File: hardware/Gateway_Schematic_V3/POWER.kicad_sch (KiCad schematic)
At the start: 49 parts, among them J3 Screw_Terminal_01x03, U11 TPS5430DDA, U4 AMS1117-3.3, U7 TPS5430DDA

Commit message: Update PCB Layout for Gateway (24/3/2026)
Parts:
- TP1, TP13: footprint TestPoint:TestPoint_Pad_D1.0mm -> IVS_NEW_FOOTPRINT:TestPoint_throughtHole_D1.0mm
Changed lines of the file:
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@@
 			)
 		)
-		(property "Footprint" "TestPoint:TestPoint_Pad_D1.0mm"
+		(property "Footprint" "IVS_NEW_FOOTPRINT:TestPoint_throughtHole_D1.0mm"
 			(at 144.145 104.14 0)
 			(effects
@@
 			)
 		)
-		(property "Footprint" "TestPoint:TestPoint_Pad_D1.0mm"
+		(property "Footprint" "IVS_NEW_FOOTPRINT:TestPoint_throughtHole_D1.0mm"
 			(at 294.005 40.64 0)
 			(effects

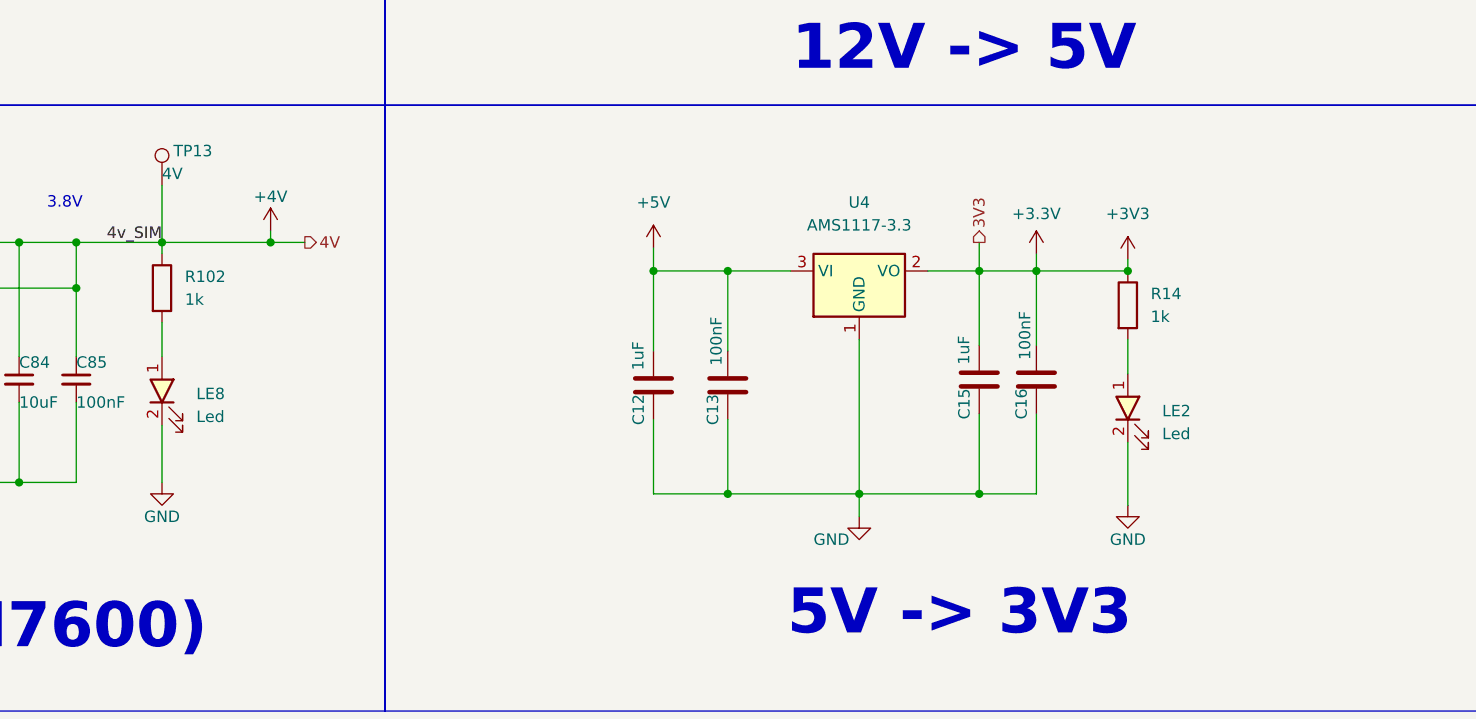
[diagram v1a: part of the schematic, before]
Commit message: Update Solder Bridge for 3v3 and 4v
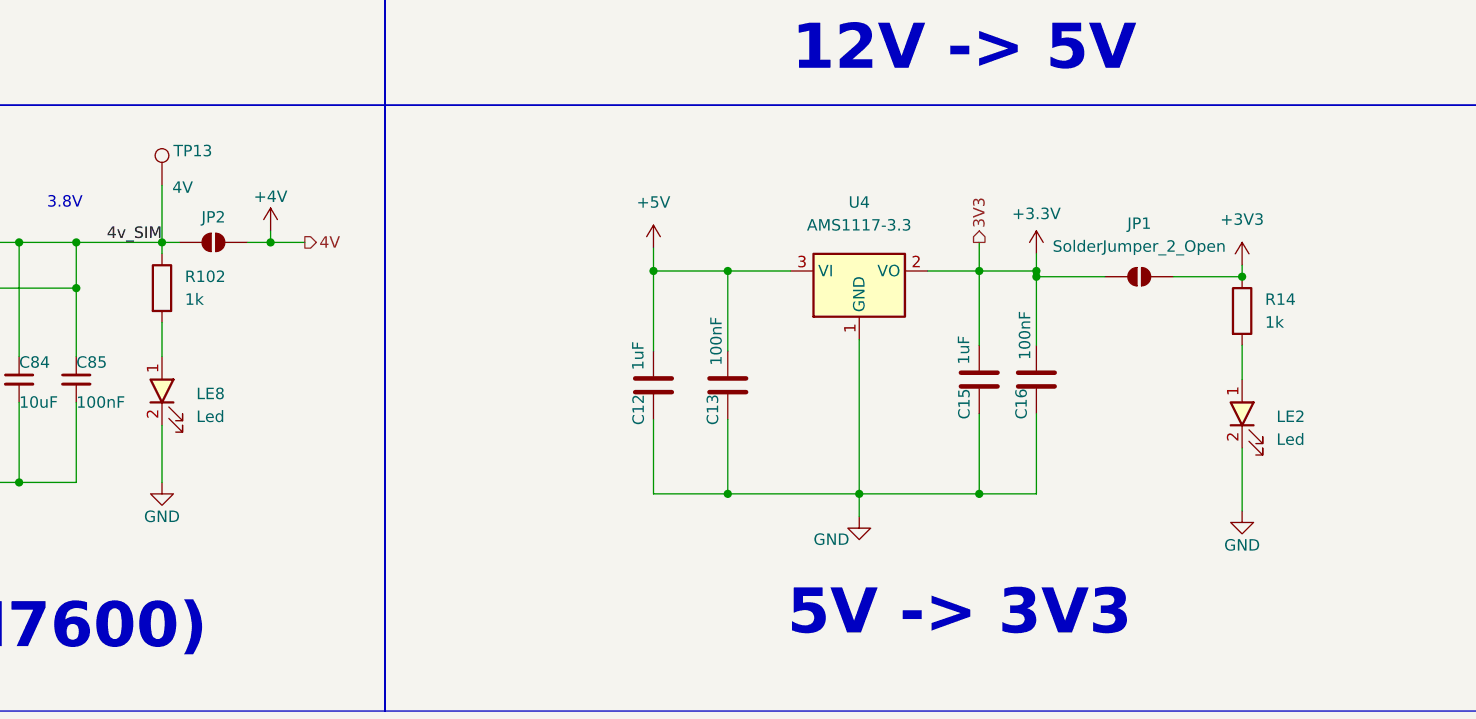
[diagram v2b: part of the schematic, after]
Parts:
- added JP1, JP2: SolderJumper_2_Open, IVS_NEW_FOOTPRINT:SolderJumper-2_P1.3mm_Open_RoundedPad1.0x1.5mm, symbol Jumper:SolderJumper_2_Open
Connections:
- net +3.3V: now also JP1.1 (A); no longer R14.1
- net +4V: now also JP2.2 (B); no longer C83.1, C84.1, C85.1, L2.2, R101.2, R102.1, TP13.1
- new net +3V3: JP1.2 (B), R14.1
- new net 4v_SIM: C83.1, C84.1, C85.1, JP2.1 (A), L2.2, R101.2, R102.1, TP13.1
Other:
- moved on the sheet: LE2, R14
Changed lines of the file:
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@@
 	)
 	(junction
+		(at 236.22 114.3)
+		(diameter 0)
+		(color 0 0 0 0)
+	)
+	(junction
 		(at 190.5 73.66)
 		(diameter 0)
@@
 	)
 	(junction
-		(at 246.38 113.665)
+		(at 259.08 114.3)
 		(diameter 0)
 		(color 0 0 0 0)
@@
 	(wire
 		(pts
-			(xy 236.22 113.665) (xy 236.22 121.92)
-		)
-		(stroke
-			(width 0)
-			(type default)
-		)
-	)
-	(wire
-		(pts
 			(xy 190.5 41.91) (xy 190.5 55.88)
 		)
@@
 	(wire
 		(pts
-			(xy 236.22 111.76) (xy 236.22 113.665)
+			(xy 139.065 104.14) (xy 139.065 110.49)
 		)
 		(stroke
@@
 	(wire
 		(pts
-			(xy 139.065 104.14) (xy 139.065 110.49)
+			(xy 86.36 53.34) (xy 90.17 53.34)
 		)
 		(stroke
@@
 		)
 	)
-	(wire
+	(polyline
 		(pts
-			(xy 86.36 53.34) (xy 90.17 53.34)
+			(xy 163.83 95.25) (xy 163.83 30.48)
 		)
 		(stroke
@@
 		)
 	)
-	(polyline
+	(wire
 		(pts
-			(xy 163.83 95.25) (xy 163.83 30.48)
+			(xy 182.88 54.61) (xy 182.88 58.42)
 		)
 		(stroke
@@
 	(wire
 		(pts
-			(xy 182.88 54.61) (xy 182.88 58.42)
+			(xy 40.64 137.16) (xy 48.26 137.16)
 		)
 		(stroke
@@
 	(wire
 		(pts
-			(xy 40.64 137.16) (xy 48.26 137.16)
+			(xy 236.22 113.665) (xy 236.22 114.3)
 		)
 		(stroke
@@
 	(wire
 		(pts
+			(xy 251.46 114.3) (xy 259.08 114.3)
+		)
+		(stroke
+			(width 0)
+			(type default)
+		)
+	)
+	(wire
+		(pts
 			(xy 182.88 41.91) (xy 190.5 41.91)
 		)
@@
 	(wire
 		(pts
-			(xy 236.22 113.665) (xy 246.38 113.665)
+			(xy 236.22 114.3) (xy 236.22 121.92)
+		)
+		(stroke
+			(width 0)
+			(type default)
+		)
+	)
+	(wire
+		(pts
+			(xy 236.22 114.3) (xy 243.84 114.3)
+		)
+		(stroke
+			(width 0)
+			(type default)
+		)
+	)
+	(wire
+		(pts
+			(xy 148.59 110.49) (xy 151.13 110.49)
 		)
 		(stroke
@@
 	(wire
 		(pts
-			(xy 139.065 110.49) (xy 151.13 110.49)
+			(xy 139.065 110.49) (xy 140.97 110.49)
 		)
 		(stroke
@@
 	(wire
 		(pts
+			(xy 236.22 111.76) (xy 236.22 113.665)
+		)
+		(stroke
+			(width 0)
+			(type default)
+		)
+	)
+	(wire
+		(pts
 			(xy 55.88 137.16) (xy 73.66 137.16)
 		)
@@
 	(wire
 		(pts
-			(xy 246.38 132.715) (xy 246.38 139.7)
+			(xy 259.08 133.35) (xy 259.08 140.335)
 		)
 		(stroke
@@
 	(wire
 		(pts
-			(xy 246.38 121.285) (xy 246.38 125.095)
+			(xy 259.08 121.92) (xy 259.08 125.73)
 		)
 		(stroke
@@
 	(wire
 		(pts
-			(xy 246.38 112.395) (xy 246.38 113.665)
+			(xy 259.08 113.03) (xy 259.08 114.3)
 		)
 		(stroke
@@
 		)
 		(property "Value" "4V"
-			(at 139.065 102.87 0)
+			(at 140.208 104.394 0)
 			(effects
 				(font
@@
 	(symbol
 		(lib_id "IVS_SYMBOLS:Led")
-		(at 246.38 130.175 90)
+		(at 259.08 130.81 90)
 		(unit 1)
 		(exclude_from_sim no)
@@
 		(fields_autoplaced yes)
 		(property "Reference" "LE2"
-			(at 250.19 129.2224 90)
+			(at 262.89 129.8574 90)
 			(effects
 				(font
@@
 		)
 		(property "Value" "Led"
-			(at 250.19 131.7624 90)
+			(at 262.89 132.3974 90)
 			(effects
 				(font
@@
 		)
 		(property "Footprint" "IVS_FOOTPRINTS:LED_0603"
-			(at 246.634 129.413 0)
+			(at 259.334 130.048 0)
 			(effects
 				(font
@@
 		)
 		(property "Datasheet" ""
-			(at 246.634 129.413 0)
+			(at 259.334 130.048 0)
 			(effects
 				(font
@@
 		)
 		(property "Description" ""
-			(at 246.38 130.175 0)
+			(at 259.08 130.81 0)
 			(effects
 				(font
@@
 	)
 	(symbol
+		(lib_id "Jumper:SolderJumper_2_Open")
+		(at 144.78 110.49 0)
+		(unit 1)
+		(exclude_from_sim yes)
+		(in_bom no)
+		(on_board yes)
+		(dnp no)
+		(property "Reference" "JP2"
+			(at 144.78 107.696 0)
+			(effects
+				(font
+					(size 1.27 1.27)
+				)
+			)
+		)
+		(property "Value" "SolderJumper_2_Open"
+			(at 149.352 107.188 0)
+			(effects
+				(font
+					(size 1.27 1.27)
+				)
+				(hide yes)
+			)
+		)
+		(property "Footprint" "IVS_NEW_FOOTPRINT:SolderJumper-2_P1.3mm_Open_RoundedPad1.0x1.5mm"
+			(at 144.78 110.49 0)
+			(effects
+				(font
+					(size 1.27 1.27)
+				)
+				(hide yes)
+			)
+		)
+		(property "Datasheet" "~"
+			(at 144.78 110.49 0)
+			(effects
+				(font
+					(size 1.27 1.27)
+				)
+				(hide yes)
+			)
+		)
+		(property "Description" "Solder Jumper, 2-pole, open"
+			(at 144.78 110.49 0)
+			(effects
+				(font
+					(size 1.27 1.27)
+				)
+				(hide yes)
+			)
+		)
+		(pin "1"
+		)
+		(pin "2"
+		)
+		(instances
+			(project "Gateway_Schematic_V3"
+				(path "/08b065f5-231d-43cb-bb9e-87dca43beac9/be7dc874-3a80-4125-bbf4-83e9b6dc8646"
+					(reference "JP2")
+					(unit 1)
+				)
+			)
+		)
+	)
+	(symbol
 		(lib_id "power:+3V3")
-		(at 246.38 112.395 0)
+		(at 259.08 113.03 0)
 		(unit 1)
 		(exclude_from_sim no)
@@
 		(fields_autoplaced yes)
 		(property "Reference" "#PWR027"
-			(at 246.38 116.205 0)
+			(at 259.08 116.84 0)
 			(effects
 				(font
@@
 		)
 		(property "Value" "+3V3"
-			(at 246.38 107.315 0)
+			(at 259.08 107.95 0)
 			(effects
 				(font
@@
 		)
 		(property "Footprint" ""
-			(at 246.38 112.395 0)
+			(at 259.08 113.03 0)
 			(effects
 				(font
@@
 		)
 		(property "Datasheet" ""
-			(at 246.38 112.395 0)
+			(at 259.08 113.03 0)
 			(effects
 				(font
@@
 		)
 		(property "Description" "Power symbol creates a global label with name \"+3V3\""
-			(at 246.38 112.395 0)
+			(at 259.08 113.03 0)
 			(effects
 				(font
@@
 	(symbol
 		(lib_id "power:GND")
-		(at 246.38 139.7 0)
+		(at 259.08 140.335 0)
 		(unit 1)
 		(exclude_from_sim no)
@@
 		(dnp no)
 		(property "Reference" "#PWR028"
-			(at 246.38 146.05 0)
+			(at 259.08 146.685 0)
 			(effects
 				(font
@@
 		)
 		(property "Value" "GND"
-			(at 246.38 143.51 0)
+			(at 259.08 144.145 0)
 			(effects
 				(font
@@
 		)
 		(property "Footprint" ""
-			(at 246.38 139.7 0)
+			(at 259.08 140.335 0)
 			(effects
 				(font
@@
 		)
 		(property "Datasheet" ""
-			(at 246.38 139.7 0)
+			(at 259.08 140.335 0)
 			(effects
 				(font
@@
 		)
 		(property "Description" "Power symbol creates a global label with name \"GND\" , ground"
-			(at 246.38 139.7 0)
+			(at 259.08 140.335 0)
 			(effects
 				(font
@@
 	)
 	(symbol
+		(lib_id "Jumper:SolderJumper_2_Open")
+		(at 247.65 114.3 0)
+		(unit 1)
+		(exclude_from_sim yes)
+		(in_bom no)
+		(on_board yes)
+		(dnp no)
+		(fields_autoplaced yes)
+		(property "Reference" "JP1"
+			(at 247.65 108.4003 0)
+			(effects
+				(font
+					(size 1.27 1.27)
+				)
+			)
+		)
+		(property "Value" "SolderJumper_2_Open"
+			(at 247.65 110.9403 0)
+			(effects
+				(font
+					(size 1.27 1.27)
+				)
+			)
+		)
+		(property "Footprint" "IVS_NEW_FOOTPRINT:SolderJumper-2_P1.3mm_Open_RoundedPad1.0x1.5mm"
+			(at 247.65 114.3 0)
+			(effects
+				(font
+					(size 1.27 1.27)
+				)
+				(hide yes)
+			)
+		)
+		(property "Datasheet" "~"
+			(at 247.65 114.3 0)
+			(effects
+				(font
+					(size 1.27 1.27)
+				)
+				(hide yes)
+			)
+		)
+		(property "Description" "Solder Jumper, 2-pole, open"
+			(at 247.65 114.3 0)
+			(effects
+				(font
+					(size 1.27 1.27)
+				)
+				(hide yes)
+			)
+		)
+		(pin "1"
+		)
+		(pin "2"
+		)
+		(instances
+			(project ""
+				(path "/08b065f5-231d-43cb-bb9e-87dca43beac9/be7dc874-3a80-4125-bbf4-83e9b6dc8646"
+					(reference "JP1")
+					(unit 1)
+				)
+			)
+		)
+	)
+	(symbol
 		(lib_id "IVS_SYMBOLS:D_Schottky")
 		(at 257.81 60.96 270)
@@
 	(symbol
 		(lib_id "Device:R")
-		(at 246.38 117.475 0)
+		(at 259.08 118.11 0)
 		(unit 1)
 		(exclude_from_sim no)
@@
 		(fields_autoplaced yes)
 		(property "Reference" "R14"
-			(at 248.92 116.2049 0)
+			(at 261.62 116.8399 0)
 			(effects
 				(font
@@
 		)
 		(property "Value" "1k"
-			(at 248.92 118.7449 0)
+			(at 261.62 119.3799 0)
 			(effects
 				(font
@@
 		)
 		(property "Footprint" "IVS_FOOTPRINTS:R_0603"
-			(at 244.602 117.475 90)
+			(at 257.302 118.11 90)
 			(effects
 				(font
@@
 		)
 		(property "Datasheet" "~"
-			(at 246.38 117.475 0)
+			(at 259.08 118.11 0)
 			(effects
 				(font
@@
 		)
 		(property "Description" "Resistor"
-			(at 246.38 117.475 0)
+			(at 259.08 118.11 0)
 			(effects
 				(font

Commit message: feat: Second review
Thay đổi kích thước chữ từ 1mm thành 0.8mm của các linh kiện - resize 1mm text size to 0.8mm
change direction of text footprint across placement direction
Note: Nhớ thay đổi footprint của nút nhấn
Thay đổi vị trí chữ để không bị chồng lấn với via
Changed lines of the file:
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@@
 		)
 		(property "Value" "0.1uF/275VAC"
-			(at 104.394 51.816 0)
+			(at 104.902 55.88 0)
 			(effects
 				(font

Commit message: Update PCB Layout after review 27/3/2026
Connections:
- net +3V3 is gone; now on net +3.3V: JP1.2 (B), R14.1
- net 4v_SIM is gone; now on net +4V: C83.1, C84.1, C85.1, JP2.1 (A), L2.2, R101.2, R102.1, TP13.1
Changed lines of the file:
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@@
 	)
 	(junction
+		(at 137.16 110.49)
+		(diameter 0)
+		(color 0 0 0 0)
+	)
+	(junction
 		(at 229.87 138.43)
 		(diameter 0)
@@
 	)
 	(junction
+		(at 254 114.3)
+		(diameter 0)
+		(color 0 0 0 0)
+	)
+	(junction
 		(at 201.93 138.43)
 		(diameter 0)
@@
 	(wire
 		(pts
+			(xy 254 114.3) (xy 259.08 114.3)
+		)
+		(stroke
+			(width 0)
+			(type default)
+		)
+	)
+	(wire
+		(pts
 			(xy 53.34 60.96) (xy 68.58 60.96)
 		)
@@
 	(wire
 		(pts
+			(xy 254 111.76) (xy 254 114.3)
+		)
+		(stroke
+			(width 0)
+			(type default)
+		)
+	)
+	(wire
+		(pts
 			(xy 198.12 54.61) (xy 198.12 41.91)
 		)
@@
 	(wire
 		(pts
+			(xy 137.16 106.68) (xy 137.16 110.49)
+		)
+		(stroke
+			(width 0)
+			(type default)
+		)
+	)
+	(wire
+		(pts
 			(xy 85.09 54.61) (xy 86.36 54.61)
 		)
@@
 	(wire
 		(pts
-			(xy 251.46 114.3) (xy 259.08 114.3)
+			(xy 251.46 114.3) (xy 254 114.3)
 		)
 		(stroke
@@
 	(wire
 		(pts
+			(xy 137.16 110.49) (xy 139.065 110.49)
+		)
+		(stroke
+			(width 0)
+			(type default)
+		)
+	)
+	(wire
+		(pts
 			(xy 48.26 123.19) (xy 48.26 137.16)
 		)
@@
 	(wire
 		(pts
-			(xy 129.54 110.49) (xy 139.065 110.49)
+			(xy 129.54 110.49) (xy 137.16 110.49)
 		)
 		(stroke
@@
 	)
 	(symbol
+		(lib_id "power:+3.3V")
+		(at 254 111.76 0)
+		(unit 1)
+		(exclude_from_sim no)
+		(in_bom yes)
+		(on_board yes)
+		(dnp no)
+		(property "Reference" "#PWR031"
+			(at 254 115.57 0)
+			(effects
+				(font
+					(size 1.27 1.27)
+				)
+				(hide yes)
+			)
+		)
+		(property "Value" "+3.3V"
+			(at 254 107.315 0)
+			(effects
+				(font
+					(size 1.27 1.27)
+				)
+			)
+		)
+		(property "Footprint" ""
+			(at 254 111.76 0)
+			(effects
+				(font
+					(size 1.27 1.27)
+				)
+				(hide yes)
+			)
+		)
+		(property "Datasheet" ""
+			(at 254 111.76 0)
+			(effects
+				(font
+					(size 1.27 1.27)
+				)
+				(hide yes)
+			)
+		)
+		(property "Description" "Power symbol creates a global label with name \"+3.3V\""
+			(at 254 111.76 0)
+			(effects
+				(font
+					(size 1.27 1.27)
+				)
+				(hide yes)
+			)
+		)
+		(pin "1"
+		)
+		(instances
+			(project "Gateway_Schematic_V3"
+				(path "/08b065f5-231d-43cb-bb9e-87dca43beac9/be7dc874-3a80-4125-bbf4-83e9b6dc8646"
+					(reference "#PWR031")
+					(unit 1)
+				)
+			)
+		)
+	)
+	(symbol
 		(lib_id "Regulator_Linear:AMS1117-3.3")
 		(at 216.535 113.665 0)
@@
 					(unit 1)
 				)
+			)
+		)
+	)
+	(symbol
+		(lib_id "power:+5V")
+		(at 137.16 106.68 0)
+		(unit 1)
+		(exclude_from_sim no)
+		(in_bom yes)
+		(on_board yes)
+		(dnp no)
+		(property "Reference" "#PWR0131"
+			(at 137.16 110.49 0)
+			(effects
+				(font
+					(size 1.27 1.27)
+				)
+				(hide yes)
+			)
+		)
+		(property "Value" "+4V"
+			(at 137.16 102.87 0)
+			(effects
+				(font
+					(size 1.27 1.27)
+				)
+			)
+		)
+		(property "Footprint" ""
+			(at 137.16 106.68 0)
+			(effects
+				(font
+					(size 1.27 1.27)
+				)
+				(hide yes)
+			)
+		)
+		(property "Datasheet" ""
+			(at 137.16 106.68 0)
+			(effects
+				(font
+					(size 1.27 1.27)
+				)
+				(hide yes)
+			)
+		)
+		(property "Description" "Power symbol creates a global label with name \"+5V\""
+			(at 137.16 106.68 0)
+			(effects
+				(font
+					(size 1.27 1.27)
+				)
+				(hide yes)
+			)
+		)
+		(pin "1"
+		)
+		(instances
+			(project "Gateway_Schematic_V3"
+				(path "/08b065f5-231d-43cb-bb9e-87dca43beac9/be7dc874-3a80-4125-bbf4-83e9b6dc8646"
+					(reference "#PWR0131")
+					(unit 1)
+				)
